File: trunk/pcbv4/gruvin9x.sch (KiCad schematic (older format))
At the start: 189 parts, among them IC1 ATMEGA2560-A_GRUVIN, K1 CONN_3, K2 CONN_3, K3 CONN_3, P1 CONN_3X2, P10 CONN_5X2, P11 CONN_1, P12 CONN_4, P13 CONN_8, P15 CONN_4, P16 CONN_1, P17 CONN_1, P18 CONN_2, P19 CONN_8, P2 CONN_5, P20 CONN_8, P21 CONN_4, P22 CONN_1, P23 CONN_1, P24 CONN_1, P3 CONN_6, P4 CONN_9, P5 CONN_9, P6 CONN_6, P7 CONN_12, P8 CONN_30_LCD_GRUVIN, P9 CONN_1, Q1 BC847C, Q2 BC847C, Q3 BC857C, Q4 BC847C, SW1 SW_PUSH, SW2 SW_PUSH, SW3 SW_PUSH, SW4 SW_PUSH, SW5 SW_PUSH, SW6 SW_PUSH, U1 78L05, U2 4066, U3 LN-6206-30, X1 16MHz 18pf

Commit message: Update of PCB V4 for vibration motor hardware
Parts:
- added C31: 0.1, symbol C
- added C32: 10u, symbol CAPAPOL
- added D16: DIODESCH, symbol DIODESCH
- added J4: JUMPER_2W, symbol JUMPER_2W
- added P14: CONN_2, symbol CONN_2
- added R15: 110K, symbol R
- added R7: 332K, symbol R
- added U4: TPS77601, symbol TPS77601
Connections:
- net labels added: VIB_OPTION
- wire segments 592 -> 615
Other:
- moved on the sheet: P20, R79

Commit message: V4 PCB - Final tweaks of the vibration motor regulator. Only leaves silkscreen labels to position and a copper pour to do, easy....
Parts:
- removed C31: 0.1, symbol C
- added C31: 47u, symbol CAPAPOL
- added C33, C34: 0.1, symbol C
- C32: value 10u -> 22u
- R91, R92, R93, R94, R95, R96: value 5K1 -> 220R
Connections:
- wire segments 615 -> 619
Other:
- moved on the sheet: C32, D16
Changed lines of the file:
@@
-EESchema Schematic File Version 2  date 25/05/2011 21:50:18
+EESchema Schematic File Version 2  date 30/05/2011 16:18:39
 LIBS:device
 LIBS:transistors
@@
 Sheet 1 1
 Title "Main Controller PCB for 100pin ATMega"
-Date "25 may 2011"
+Date "30 may 2011"
 Rev "4.0"
 Comp ""
@@
 Comment4 "Licensed under the TAPR Open Hardware License (see file,  LICENSE)"
 $EndDescr
-Connection ~ 14600 13200
-Wire Wire Line
-	14600 13250 14600 13200
-Connection ~ 17700 13200
-Wire Wire Line
-	17700 13300 17700 13200
+Wire Wire Line
+	14700 13650 14400 13650
+Connection ~ 14700 13200
+Wire Wire Line
+	14700 13250 14700 13200
+Connection ~ 17500 13200
+Wire Wire Line
+	17500 13350 17500 13200
+Connection ~ 17850 14350
+Wire Wire Line
+	17850 13750 17850 14350
+Wire Wire Line
+	16950 14350 18250 14350
 Wire Wire Line
 	16950 13850 16950 13750
 Wire Wire Line
-	16300 13200 18250 13200
-Wire Wire Line
-	14600 13650 14600 13800
-Wire Wire Line
-	17200 13750 17200 14500
+	17200 14500 17200 13750
 Wire Wire Line
 	15650 14050 15650 14150
@@
 	6400 13750 6050 13750
 Wire Wire Line
-	7450 14550 7750 14550
+	7750 14550 7450 14550
 Wire Wire Line
 	6700 6000 6700 5900
@@
 	8400 8550 8500 8550
 Wire Wire Line
-	7850 8750 7850 8500
+	7850 8500 7850 8750
 Wire Wire Line
 	13800 9650 13850 9650
@@
 	14450 11550 16100 11550
 Wire Wire Line
-	13750 11550 13950 11550
+	13950 11550 13750 11550
 Wire Wire Line
 	13650 12350 13650 12200
@@
 	11850 3100 11850 3050
 Wire Wire Line
-	11950 5000 10900 5000
+	10900 5000 11950 5000
 Wire Wire Line
 	9900 4700 9900 2750
@@
 	4550 12050 3950 12050
 Wire Wire Line
-	16750 7100 18450 7100
+	18450 7100 16750 7100
 Wire Wire Line
 	13100 7650 12150 7650
@@
 Connection ~ 14100 2550
 Wire Wire Line
-	15100 2550 13500 2550
-Wire Wire Line
-	14550 3050 13500 3050
+	13500 2550 15100 2550
+Wire Wire Line
+	13500 3050 14550 3050
 Wire Wire Line
 	9000 10850 10650 10850
@@
 	11600 3750 11950 3750
 Wire Wire Line
-	10200 3550 10200 3350
+	10200 3350 10200 3550
 Connection ~ 10800 4400
 Wire Wire Line
@@
 	10650 3750 10650 3850
 Wire Wire Line
-	11100 3750 10500 3750
+	10500 3750 11100 3750
 Wire Wire Line
 	11500 5300 11500 5200
@@
 	6400 10950 5950 10950
 Wire Wire Line
-	15800 9850 15800 9600
+	15800 9600 15800 9850
 Connection ~ 5500 2650
 Wire Wire Line
@@
 	15850 10850 16100 10850
 Wire Wire Line
-	16100 10700 14800 10700
+	14800 10700 16100 10700
 Connection ~ 15950 12000
 Wire Wire Line
@@
 Connection ~ 15800 9100
 Wire Wire Line
-	15800 9000 15800 9200
-Wire Wire Line
-	16100 9400 16700 9400
+	15800 9200 15800 9000
+Wire Wire Line
+	16700 9400 16100 9400
 Wire Wire Line
 	19100 8650 17300 8650
@@
 Connection ~ 17550 7650
 Wire Wire Line
-	17600 7650 17150 7650
+	17150 7650 17600 7650
 Wire Wire Line
 	19050 6800 18000 6800
@@
 	5500 3900 5500 3800
 Wire Wire Line
-	4800 3200 4800 3350
+	4800 3350 4800 3200
 Connection ~ 5150 2650
 Wire Wire Line
@@
 Connection ~ 4800 3300
 Wire Wire Line
-	5500 3300 5500 3200
+	5500 3200 5500 3300
 Wire Wire Line
 	6400 3200 6400 2950
@@
 	7350 3300 7350 3200
 Wire Wire Line
-	7000 3200 7000 3350
+	7000 3350 7000 3200
 Wire Wire Line
 	7000 2800 7000 2650
@@
 	15950 11700 16100 11700
 Wire Wire Line
-	15750 11100 15950 11100
+	15950 11100 15750 11100
 Wire Wire Line
 	14750 11100 15150 11100
@@
 Connection ~ 15850 10700
 Wire Wire Line
-	4350 2650 6000 2650
+	6000 2650 4350 2650
 Wire Wire Line
 	9350 3600 9350 3450
@@
 	16250 7650 16250 7600
 Wire Wire Line
-	19100 8850 17300 8850
+	17300 8850 19100 8850
 Wire Wire Line
 	18650 10650 18650 9150
@@
 	17250 6100 17250 7750
 Wire Wire Line
-	10900 5100 11950 5100
-Wire Wire Line
-	10950 3850 10950 3750
+	11950 5100 10900 5100
+Wire Wire Line
+	10950 3750 10950 3850
 Connection ~ 10950 3750
 Wire Wire Line
@@
 	13450 11350 13450 11250
 Wire Wire Line
-	14900 9850 14400 9850
+	14400 9850 14900 9850
 Wire Wire Line
 	14450 9850 14450 9700
@@
 	13950 8750 13950 8650
 Wire Wire Line
-	15150 12150 14200 12150
+	14200 12150 15150 12150
 Wire Wire Line
 	6400 13650 5200 13650
@@
 	7550 7900 7550 8750
 Wire Wire Line
-	7450 7750 7450 8750
+	7450 8750 7450 7750
 Wire Wire Line
 	15850 10250 17900 10250
@@
 Connection ~ 7650 14550
 Wire Wire Line
-	7550 14850 7550 14550
+	7550 14550 7550 14850
 Wire Wire Line
 	6400 10650 6100 10650
@@
 	14350 7900 15300 7900
 Wire Wire Line
-	16300 13200 16300 13300
+	16300 13300 16300 13200
 Wire Wire Line
 	15000 13300 15000 13200
@@
 Connection ~ 17200 14350
 Wire Wire Line
-	18250 13200 18250 13250
-Wire Wire Line
-	17700 13700 17700 14350
+	18250 13250 18250 13200
 Wire Wire Line
 	17200 13200 17200 13350
@@
 	16700 13750 16700 13500
 Wire Wire Line
-	18250 13450 18250 14350
-Wire Wire Line
-	18250 14350 16950 14350
-Connection ~ 17700 14350
+	18250 14350 18250 13450
+Wire Wire Line
+	18250 13200 16300 13200
+Wire Wire Line
+	17500 13750 17500 14350
+Connection ~ 17500 14350
+Wire Wire Line
+	17850 13350 17850 13200
+Connection ~ 17850 13200
+Wire Wire Line
+	14400 13200 14400 13250
+Wire Wire Line
+	14400 13650 14400 13800
+$Comp
+L C C34
+U 1 1 4DE3AEF0
+P 17500 13550
+F 0 "C34" H 17400 13450 50  0000 L CNN
+F 1 "0.1" H 17350 13650 50  0000 L CNN
+	1    17500 13550
+	-1   0    0    1
+$EndComp
+$Comp
+L C C33
+U 1 1 4DE3AEE4
+P 14700 13450
+F 0 "C33" H 14600 13350 50  0000 L CNN
+F 1 "0.1" H 14550 13550 50  0000 L CNN
+	1    14700 13450
+	-1   0    0    1
+$EndComp
+$Comp
+L CAPAPOL C31
+U 1 1 4DE3AC28
+P 17200 13550
+F 0 "C31" H 17100 13450 50  0000 L CNN
+F 1 "47u" H 17050 13700 50  0000 L CNN
+	1    17200 13550
+	-1   0    0    1
+$EndComp
 $Comp
 L GND #PWR01
 U 1 1 4DDD6233
-P 14600 13800
-F 0 "#PWR01" H 14600 13800 30  0001 C CNN
-F 1 "GND" H 14600 13730 30  0001 C CNN
-	1    14600 13800
-	1    0    0    -1
-$EndComp
-$Comp
-L C C31
-U 1 1 4DDD6225
-P 14600 13450
-F 0 "C31" V 14550 13300 50  0000 L CNN
-F 1 "0.1" V 14650 13350 50  0000 L CNN
-	1    14600 13450
+P 14400 13800
+F 0 "#PWR01" H 14400 13800 30  0001 C CNN
+F 1 "GND" H 14400 13730 30  0001 C CNN
+	1    14400 13800
 	1    0    0    -1
 $EndComp
@@
 L DIODESCH D16
 U 1 1 4DDD61E7
-P 17700 13500
-F 0 "D16" H 17700 13600 40  0000 C CNN
-F 1 "DIODESCH" H 17700 13400 40  0000 C CNN
-	1    17700 13500
+P 17850 13550
+F 0 "D16" H 17850 13650 40  0000 C CNN
+F 1 "DIODESCH" H 17850 13450 40  0000 C CNN
+	1    17850 13550
 	0    1    -1   0
 $EndComp
@@
 L CAPAPOL C32
 U 1 1 4DDD61B4
-P 17200 13550
-F 0 "C32" H 17100 13450 50  0000 L CNN
-F 1 "10u" H 17050 13700 50  0000 L CNN
-	1    17200 13550
+P 14400 13450
+F 0 "C32" H 14300 13350 50  0000 L CNN
+F 1 "22u" H 14250 13600 50  0000 L CNN
+	1    14400 13450
 	-1   0    0    1
 $EndComp
@@
 P 6100 6400
 F 0 "R96" V 6180 6400 50  0000 C CNN
-F 1 "5K1" V 6100 6400 50  0000 C CNN
+F 1 "220R" V 6100 6400 50  0000 C CNN
 	1    6100 6400
 	0    1    1    0
@@
 P 6550 6300
 F 0 "R95" V 6630 6300 50  0000 C CNN
-F 1 "5K1" V 6550 6300 50  0000 C CNN
+F 1 "220R" V 6550 6300 50  0000 C CNN
 	1    6550 6300
 	0    1    1    0
@@
 P 6500 7300
 F 0 "R94" V 6580 7300 50  0000 C CNN
-F 1 "5K1" V 6500 7300 50  0000 C CNN
+F 1 "220R" V 6500 7300 50  0000 C CNN
 	1    6500 7300
 	0    1    1    0
@@
 P 6550 6500
 F 0 "R93" V 6630 6500 50  0000 C CNN
-F 1 "5K1" V 6550 6500 50  0000 C CNN
+F 1 "220R" V 6550 6500 50  0000 C CNN
 	1    6550 6500
 	0    1    1    0
@@
 P 6100 7200
 F 0 "R92" V 6180 7200 50  0000 C CNN
-F 1 "5K1" V 6100 7200 50  0000 C CNN
+F 1 "220R" V 6100 7200 50  0000 C CNN
 	1    6100 7200
 	0    1    1    0
@@
 P 6500 7100
 F 0 "R91" V 6580 7100 50  0000 C CNN
-F 1 "5K1" V 6500 7100 50  0000 C CNN
+F 1 "220R" V 6500 7100 50  0000 C CNN
 	1    6500 7100
 	0    1    1    0

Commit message: Final "Maybe" PCB V4 change, the 4066 is gone
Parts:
- removed C18: 0.1, symbol C
- removed R33, R34: 10K, symbol R
- removed U2: 4066, symbol 4066
- added Q5, Q6, Q7: BC847C, SOT23-BCE, symbol BC847C
- added Q8: BC857C, SOT23-BCE, symbol BC857C
- added R16, R17, R23, R24, R27, R28: 5K1, symbol R
- added R29, R30: 200R, symbol R
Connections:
- net labels added: Module_PPM
- wire segments 619 -> 632
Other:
- moved on the sheet: C31, C32, C33, C34, D16, J4, P14, Q4, R15, R7, R79, R80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

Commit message: Changes to the PPM I/O section of the V4 PCB
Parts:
- removed Q6: BC847C, SOT23-BCE, symbol BC847C
- removed Q8: BC857C, SOT23-BCE, symbol BC857C
- removed R17, R24: 5K1, symbol R
- removed R79: 200, symbol R
- added C18, C35: 47u, symbol CAPAPOL
- added D17: DIODESCH, symbol DIODESCH
- R29, R30: value 200R -> 100R
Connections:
- wire segments 632 -> 623
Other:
- moved on the sheet: R27, R28, R29, R30

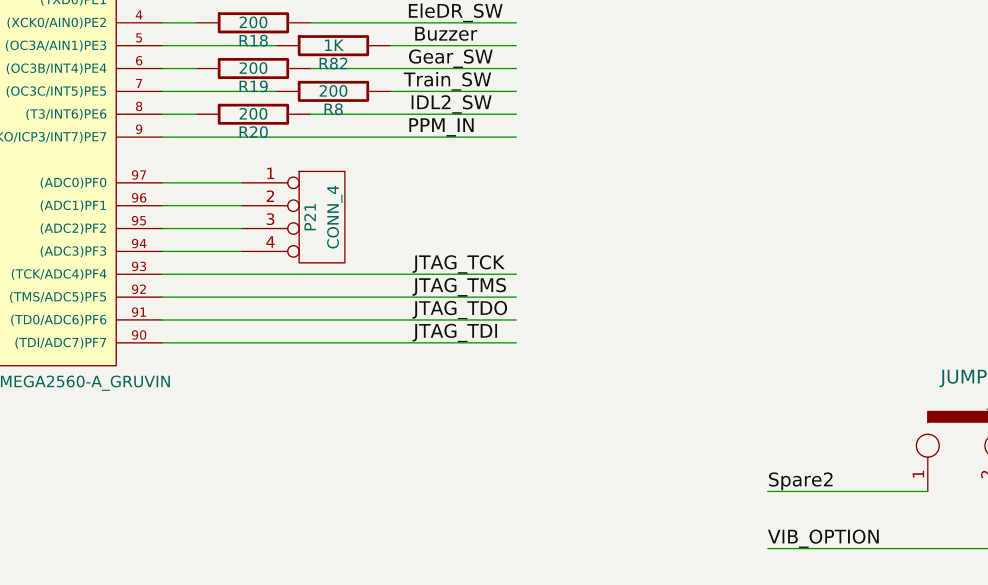
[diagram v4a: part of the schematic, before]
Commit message: Added some voltage dividers to two the spare ADC pins, possibly for individual LiPo cell voltage monitoring.
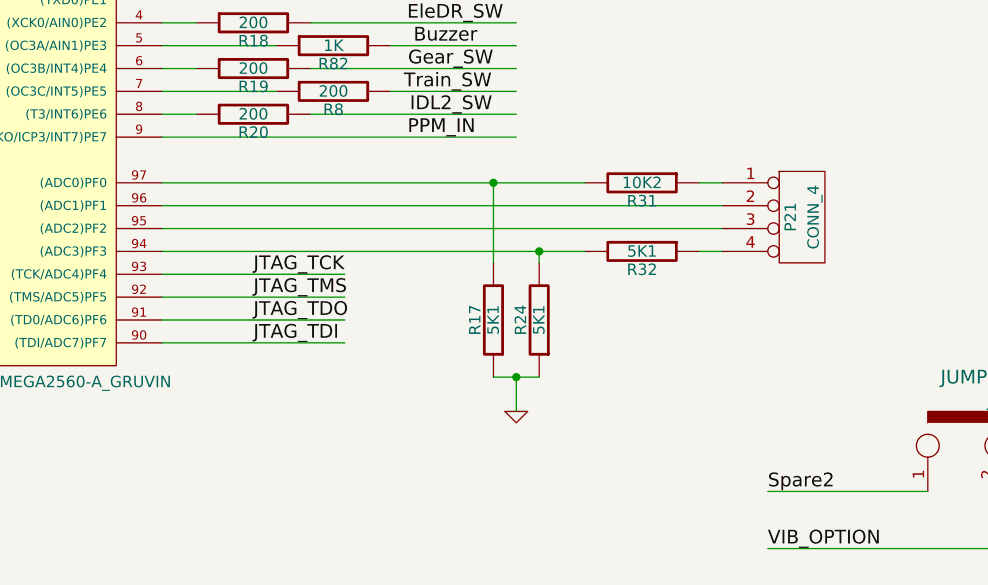
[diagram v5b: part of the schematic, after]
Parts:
- added R17, R24, R32: 5K1, symbol R
- added R31: 10K2, symbol R
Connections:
- wire segments 623 -> 629
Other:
- moved on the sheet: P21

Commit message: Thought is more sensible to have voltage dividers on all the spare ADC channels, keeping them all the same ratio saves on code, and saves damage if they get connected wrongly to a Tx LiPo pack.
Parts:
- added R33, R77: 5K1, symbol R
- added R34, R79: 10K2, symbol R
- R32: value 5K1 -> 10K2
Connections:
- wire segments 629 -> 633
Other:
- moved on the sheet: R31

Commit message: Added breakout for AGND, GND, and Vcc to V4 PCB
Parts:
- added K4: CONN_3, symbol CONN_3
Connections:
- wire segments 633 -> 639

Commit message: Added a filter cap around Q1 to try and stop spurious switching when the buzzer sounds.
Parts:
- added C36: 0.1, symbol C
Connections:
- wire segments 639 -> 641
